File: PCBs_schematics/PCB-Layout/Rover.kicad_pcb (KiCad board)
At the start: 2 copper layers, 93 x 135 mm, 49 parts, among them J1 ToF-sensor2, J2 Pi-15,17, J3 Conn_01x02, J4 Conn_01x04, J5 Conn_01x04, J6 Conn_01x03, J7 USB-conn, M1 Sensor-DC-motor, M2 Wheel-dc-motor, M3 Motor_Servo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

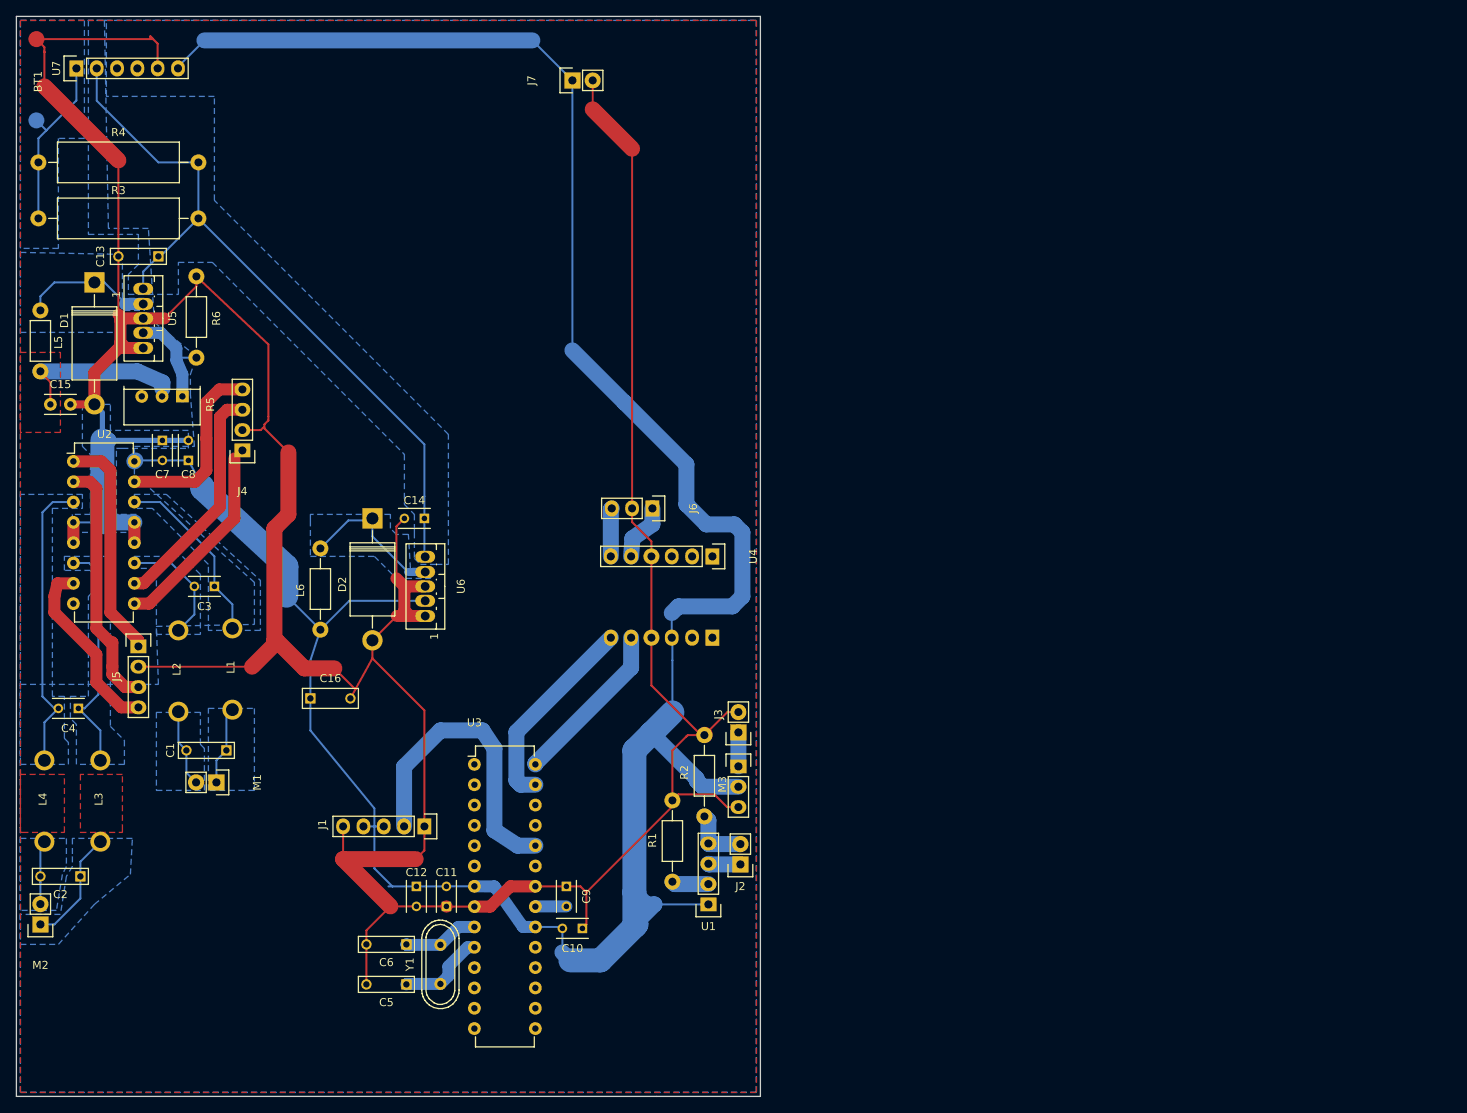
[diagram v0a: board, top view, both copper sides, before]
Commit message: added building instructions for the Rover
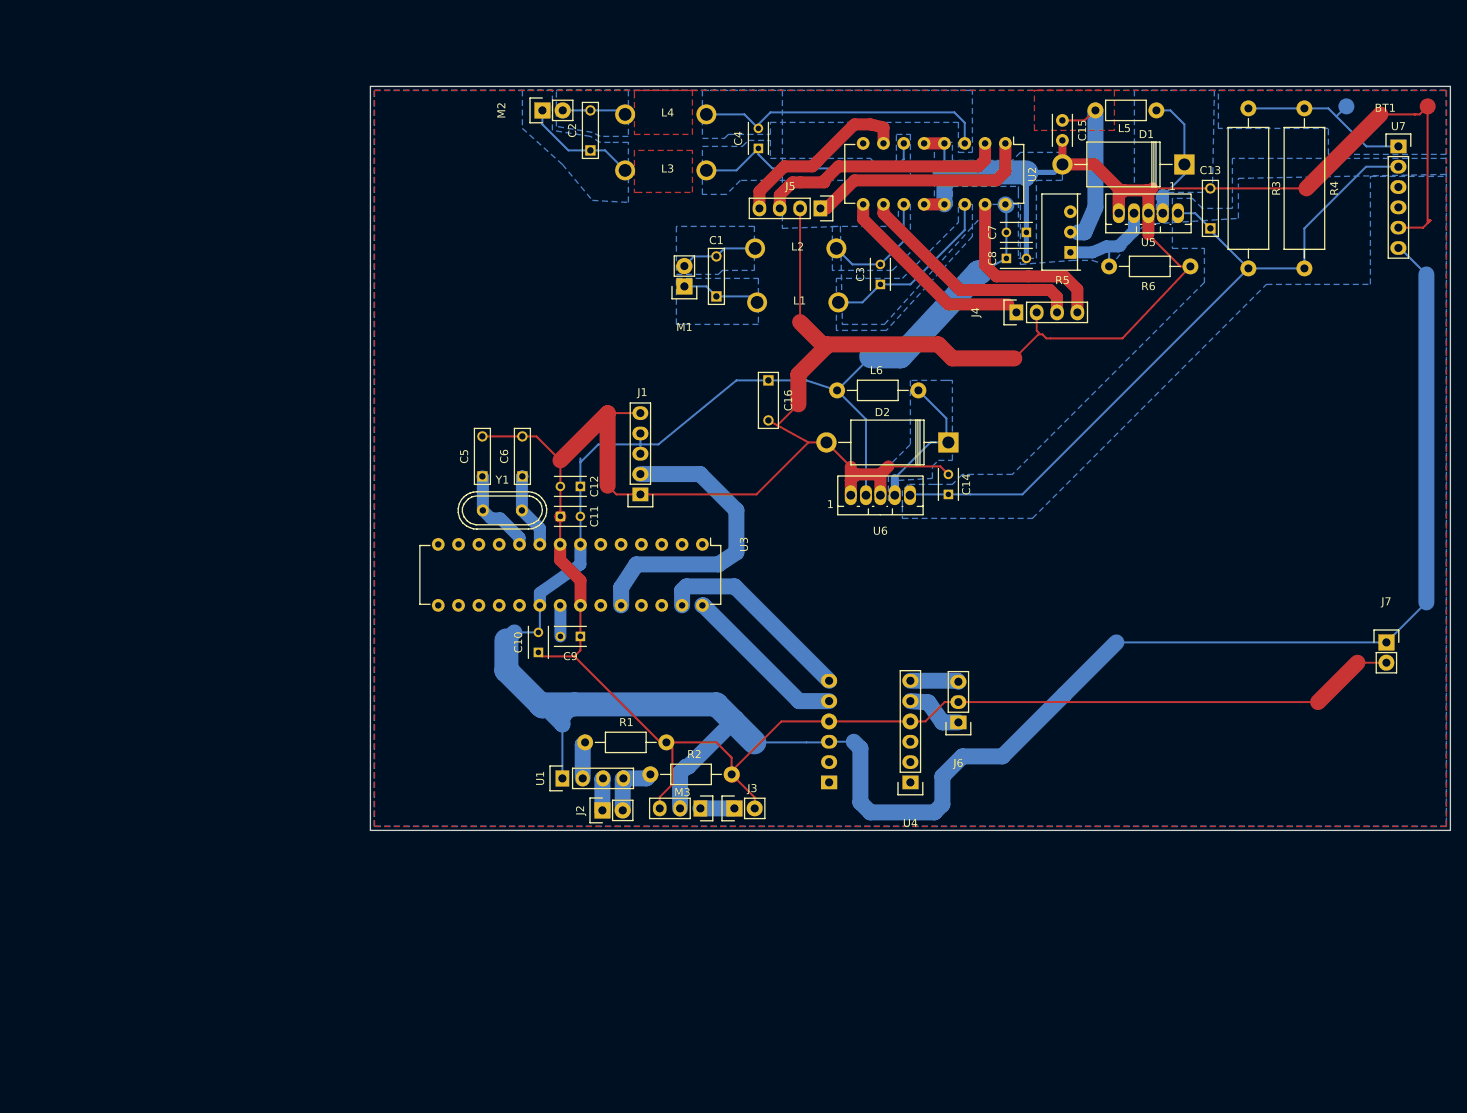
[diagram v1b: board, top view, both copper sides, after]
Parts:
- moved U7 165.5 mm to (196.5, 51.5), turned to 0 degrees
- moved BT1 163.8 mm to (190.0, 46.5), turned to 0 degrees
- moved R4 158.4 mm to (184.8, 46.8), turned to 270 degrees
- moved R3 151.9 mm to (177.8, 46.8), turned to 270 degrees
- moved L5 141.7 mm to (166.2, 47.0), turned to 180 degrees
- moved D1 137.0 mm to (169.8, 53.8), turned to 180 degrees
- moved C13 131.5 mm to (173.0, 61.8), turned to 90 degrees
- moved C15 131.4 mm to (154.5, 48.2), turned to 270 degrees
- moved U5 127.0 mm to (165.2, 59.2), turned to 180 degrees
- moved R6 124.3 mm to (170.5, 66.5), turned to 180 degrees
- moved J7 123.6 mm to (195.0, 113.5), turned to 0 degrees
- moved U2 123.1 mm to (147.4, 51.1), turned to 270 degrees
- moved M2 119.5 mm to (89.5, 47.0), turned to 90 degrees
- moved L4 115.6 mm to (110.0, 47.5), turned to 180 degrees
- moved R5 112.4 mm to (155.5, 64.8), turned to 90 degrees
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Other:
- board size 93 x 135 mm -> 135 x 93 mm
